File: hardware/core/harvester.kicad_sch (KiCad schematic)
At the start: 28 parts, among them J2 Conn_01x02_Pin, U2 BQ25173DSG, U3 BQ25570, U5 AXP1T34

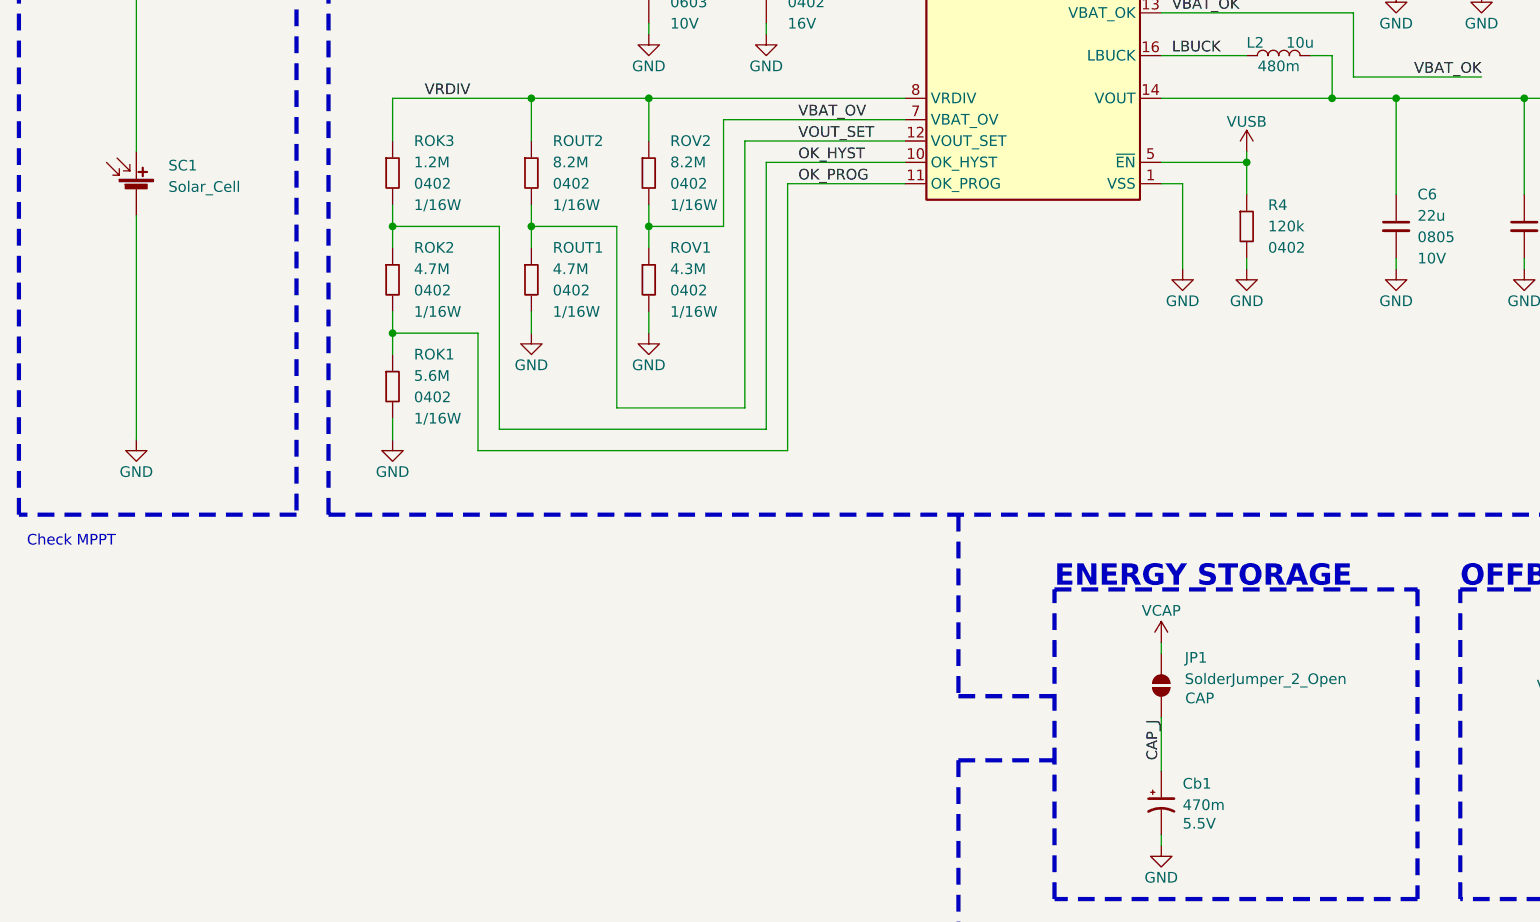
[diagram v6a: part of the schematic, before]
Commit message: updated harvester configuration resistors and removed cap solder link
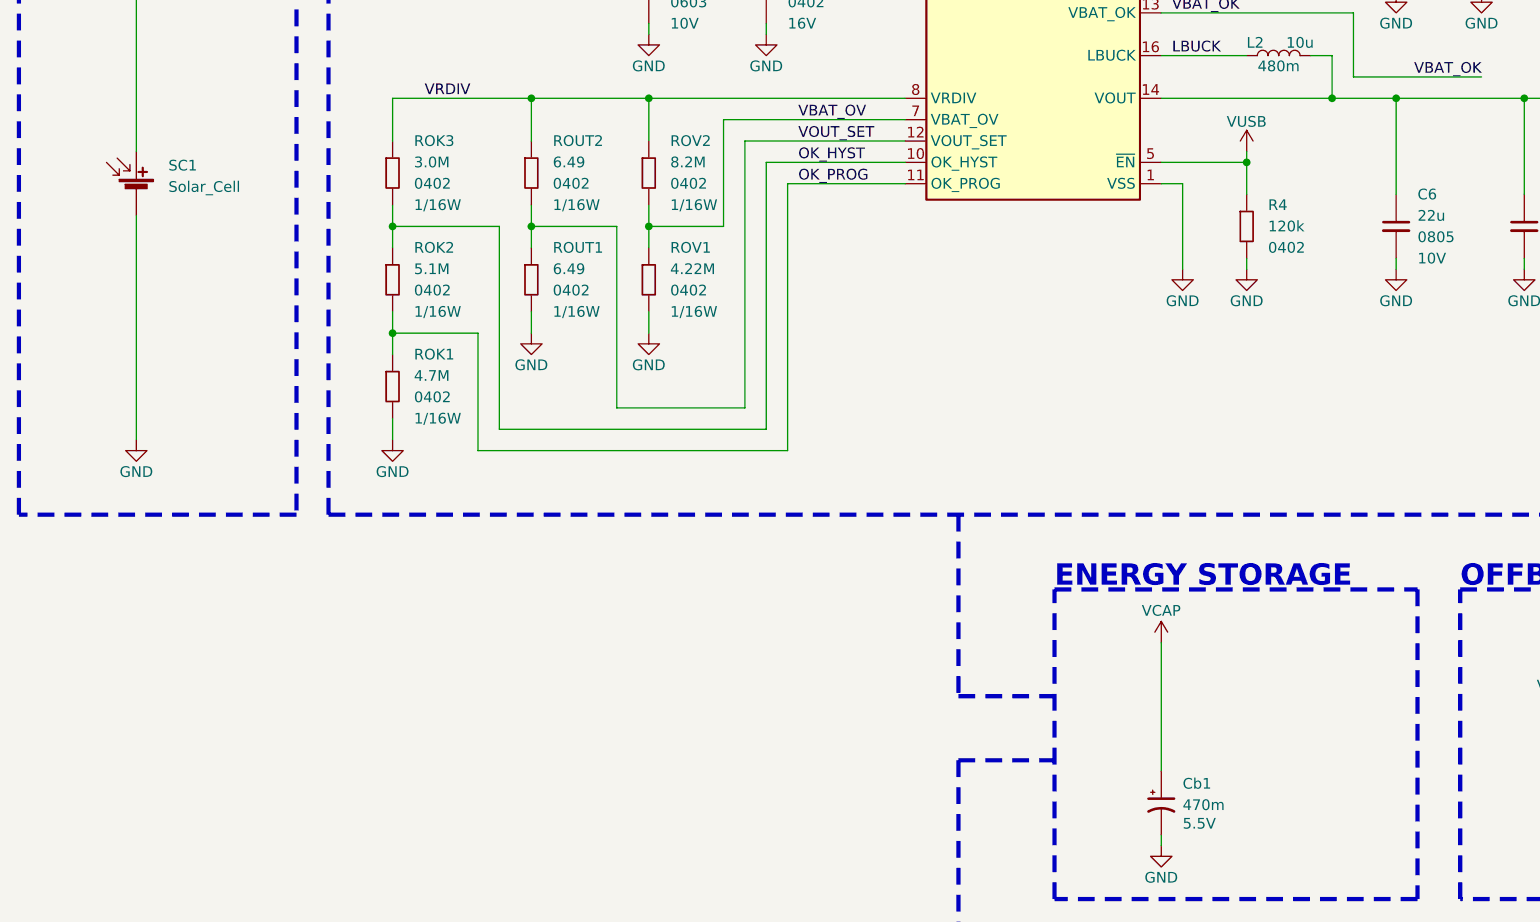
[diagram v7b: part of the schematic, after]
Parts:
- removed JP1: SolderJumper_2_Open, misc:SolderJumper2_Open_0402, symbol misc:SolderJumper_2_Open
- ROK1: value 5.6M -> 4.7M; Part Number RC0402FR-075M6L -> RC0402FR-074M7L
- ROK2: value 4.7M -> 5.1M; Part Number RC0402FR-074M7L -> RC0402FR-075M1L
- ROK3: value 1.2M -> 3.0M; Part Number RC0402FR-071M2L -> RC0402FR-073ML
- ROUT1: value 4.7M -> 6.49; Part Number RC0402FR-074M7L -> RC0402FR-076M49L
- ROUT2: value 8.2M -> 6.49; Part Number RC0402FR-078M2L -> RC0402FR-076M49L
- ROV1: value 4.3M -> 4.22M; Part Number RC0402FR-074M3L -> RC0402FR-074M22L
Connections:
- net CAP_J is gone; now on net VCAP: Cb1.1
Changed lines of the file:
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@@
 		)
 	)
-	(text_box "Check MPPT"
-		(exclude_from_sim no)
-		(at 16.51 107.95 0)
-		(size 92.71 7.62)
-		(margins 0.9525 0.9525 0.9525 0.9525)
-		(stroke
-			(width -0.0001)
-			(type solid)
-		)
-		(fill
-			(type color)
-			(color 255 0 0 1)
-		)
-		(effects
-			(font
-				(size 1.27 1.27)
-				(color 255 255 255 1)
-			)
-			(justify left top)
-		)
-	)
 	(junction
 		(at 161.29 34.29)
@@
 	(wire
 		(pts
-			(xy 152.4 121.92) (xy 152.4 123.19)
+			(xy 152.4 121.92) (xy 152.4 137.16)
 		)
 		(stroke
@@
 	(wire
 		(pts
-			(xy 152.4 130.81) (xy 152.4 137.16)
-		)
-		(stroke
-			(width 0)
-			(type default)
-		)
-	)
-	(wire
-		(pts
 			(xy 60.96 57.15) (xy 60.96 62.23)
 		)
@@
 		)
 	)
-	(label "CAP_J"
-		(at 152.4 135.89 90)
-		(effects
-			(font
-				(size 1.27 1.27)
-			)
-			(justify left bottom)
-		)
-	)
 	(label "VREF_SAMP"
 		(at 109.22 39.37 0)
@@
 			)
 		)
-		(property "Datasheet" ""
+		(property "Datasheet" "https://search.murata.co.jp/Ceramy/image/img/A01X/G101/ENG/GRM155Z71A105KE01-01A.pdf"
 			(at 195.58 68.58 0)
 			(effects
@@
 			)
 		)
-		(property "Datasheet" ""
+		(property "Datasheet" "https://www.yageo.com/upload/media/product/products/datasheet/rchip/PYu-RC_Group_51_RoHS_L_12.pdf"
 			(at 91.44 62.23 0)
 			(effects
@@
 			)
 		)
-		(property "Description" "Capacitor 470mF throug-hole"
+		(property "Description" "Capacitor 470mF through-hole"
 			(at 152.4 137.16 0)
 			(effects
@@
 			)
 		)
-		(property "Value" "8.2M"
+		(property "Value" "6.49"
 			(at 80.01 64.7699 0)
 			(effects
@@
 			)
 		)
-		(property "Datasheet" ""
+		(property "Datasheet" "https://www.yageo.com/upload/media/product/products/datasheet/rchip/PYu-RC_Group_51_RoHS_L_12.pdf"
 			(at 77.47 62.23 0)
 			(effects
@@
 			)
 		)
-		(property "Part Number" "RC0402FR-078M2L"
+		(property "Part Number" "RC0402FR-076M49L"
 			(at 77.47 62.23 0)
 			(effects
@@
 			)
 		)
-		(property "Datasheet" ""
+		(property "Datasheet" "https://www.yageo.com/upload/media/product/products/datasheet/rchip/PYu-RC_Group_51_RoHS_L_12.pdf"
 			(at 153.67 180.34 0)
 			(effects
@@
 			)
 		)
-		(property "Value" "4.3M"
+		(property "Value" "4.22M"
 			(at 93.98 77.4699 0)
 			(effects
@@
 			)
 		)
-		(property "Datasheet" ""
+		(property "Datasheet" "https://www.yageo.com/upload/media/product/products/datasheet/rchip/PYu-RC_Group_51_RoHS_L_12.pdf"
 			(at 91.44 74.93 0)
 			(effects
@@
 			)
 		)
-		(property "Part Number" "RC0402FR-074M3L"
+		(property "Part Number" "RC0402FR-074M22L"
 			(at 91.44 74.93 0)
 			(effects
@@
 			)
 		)
-		(property "Datasheet" ""
+		(property "Datasheet" "https://search.murata.co.jp/Ceramy/image/img/A01X/G101/ENG/GRM188Z71A475ME15-01.pdf"
 			(at 180.34 35.56 0)
 			(effects
@@
 			)
 		)
-		(property "Datasheet" ""
+		(property "Datasheet" "https://mm.digikey.com/Volume0/opasdata/d220001/medias/docus/610/NRS4012T220MDGJ_SS.pdf"
 			(at 101.6 34.29 0)
 			(effects
@@
 			)
 		)
-		(property "Datasheet" ""
+		(property "Datasheet" "https://search.murata.co.jp/Ceramy/image/img/A01X/G101/ENG/GRM188Z71A475ME15-01.pdf"
 			(at 91.44 40.64 0)
 			(effects
@@
 			)
 		)
-		(property "Datasheet" ""
+		(property "Datasheet" "https://www.precidip.com/AppHost/9696,1/Scripts/Modules/Catalog/Default.aspx?c=7&i=223&p=86&pdf=1&dsku=801-PP-NNN-20-001101"
 			(at 210.82 135.89 0)
 			(effects
@@
 			)
 		)
-		(property "Description" "Generic connector, single row, 01x02, script generated"
+		(property "Description" "Right angle 2.54mm connector"
 			(at 210.82 135.89 0)
 			(effects
@@
 			)
 		)
-		(property "Datasheet" ""
+		(property "Datasheet" "https://search.murata.co.jp/Ceramy/image/img/A01X/G101/ENG/GRM155Z71A105KE01-01A.pdf"
 			(at 165.1 180.34 0)
 			(effects
@@
 			)
 		)
-		(property "Description" "Inductor 10u 1008Metric"
+		(property "Description" "Inductor 10u"
 			(at 166.116 56.134 0)
 			(effects
@@
 			)
 		)
-		(property "Value" "5.6M"
+		(property "Value" "4.7M"
 			(at 63.5 90.1699 0)
 			(effects
@@
 			)
 		)
-		(property "Datasheet" ""
+		(property "Datasheet" "https://www.yageo.com/upload/media/product/products/datasheet/rchip/PYu-RC_Group_51_RoHS_L_12.pdf"
 			(at 60.96 87.63 0)
 			(effects
@@
 			)
 		)
-		(property "Part Number" "RC0402FR-075M6L"
+		(property "Part Number" "RC0402FR-074M7L"
 			(at 60.96 87.63 0)
 			(effects
@@
 			)
 		)
-		(property "Datasheet" ""
+		(property "Datasheet" "https://search.murata.co.jp/Ceramy/image/img/A01X/G101/ENG/GRM155Z71A105KE01-01A.pdf"
 			(at 96.52 180.34 0)
 			(effects
@@
 			)
 		)
-		(property "Datasheet" ""
+		(property "Datasheet" "https://search.murata.co.jp/Ceramy/image/img/A01X/G101/ENG/GRM155R71C103KA01-01.pdf"
 			(at 105.41 40.64 0)
 			(effects
@@
 			)
 		)
-		(property "Datasheet" ""
+		(property "Datasheet" "https://www.yageo.com/upload/media/product/products/datasheet/rchip/PYu-RC_Group_51_RoHS_L_12.pdf"
 			(at 153.67 170.18 0)
 			(effects
@@
 			)
 		)
-		(property "Datasheet" ""
+		(property "Datasheet" "https://search.murata.co.jp/Ceramy/image/img/A01X/G101/ENG/GRM21BZ71A226ME15-01.pdf"
 			(at 180.34 68.58 0)
 			(effects
@@
 			)
 		)
-		(property "Value" "4.7M"
+		(property "Value" "5.1M"
 			(at 63.5 77.4699 0)
 			(effects
@@
 			)
 		)
-		(property "Datasheet" ""
+		(property "Datasheet" "https://www.yageo.com/upload/media/product/products/datasheet/rchip/PYu-RC_Group_51_RoHS_L_12.pdf"
 			(at 60.96 74.93 0)
 			(effects
@@
 			)
 		)
-		(property "Part Number" "RC0402FR-074M7L"
+		(property "Part Number" "RC0402FR-075M1L"
 			(at 60.96 74.93 0)
 			(effects
@@
 			)
 		)
-		(property "Value" "1.2M"
+		(property "Value" "3.0M"
 			(at 63.5 64.7699 0)
 			(effects
@@
 			)
 		)
-		(property "Datasheet" ""
+		(property "Datasheet" "https://www.yageo.com/upload/media/product/products/datasheet/rchip/PYu-RC_Group_51_RoHS_L_12.pdf"
 			(at 60.96 62.23 0)
 			(effects
@@
 			)
 		)
-		(property "Part Number" "RC0402FR-071M2L"
+		(property "Part Number" "RC0402FR-073ML"
 			(at 60.96 62.23 0)
 			(effects
@@
 			)
 		)
-		(property "Value" "4.7M"
+		(property "Value" "6.49"
 			(at 80.01 77.4699 0)
 			(effects
@@
 			)
 		)
-		(property "Datasheet" ""
+		(property "Datasheet" "https://www.yageo.com/upload/media/product/products/datasheet/rchip/PYu-RC_Group_51_RoHS_L_12.pdf"
 			(at 77.47 74.93 0)
 			(effects
@@
 			)
 		)
-		(property "Part Number" "RC0402FR-074M7L"
+		(property "Part Number" "RC0402FR-076M49L"
 			(at 77.47 74.93 0)
 			(effects
@@
 			)
 		)
-		(property "Datasheet" ""
+		(property "Datasheet" "https://www.yageo.com/upload/media/product/products/datasheet/rchip/PYu-RC_Group_51_RoHS_L_12.pdf"
 			(at 162.56 68.58 0)
 			(effects
@@
 			)
 		)
-		(property "Datasheet" ""
+		(property "Datasheet" "https://search.murata.co.jp/Ceramy/image/img/A01X/G101/ENG/GRM155R71C103KA01-01.pdf"
 			(at 190.5 35.56 0)
 			(effects
@@
 	)
 	(symbol
-		(lib_id "misc:SolderJumper_2_Open")
-		(at 152.4 127 90)
-		(unit 1)
-		(exclude_from_sim no)
-		(in_bom no)
-		(on_board yes)
-		(dnp no)
-		(property "Reference" "JP1"
-			(at 155.194 123.698 90)
-			(effects
-				(font
-					(size 1.27 1.27)
-				)
-				(justify right)
-			)
-		)
-		(property "Value" "SolderJumper_2_Open"
-			(at 155.194 126.238 90)
-			(effects
-				(font
-					(size 1.27 1.27)
-				)
-				(justify right)
-			)
-		)
-		(property "Footprint" "misc:SolderJumper2_Open_0402"
-			(at 152.4 127 0)
-			(effects
-				(font
-					(size 1.27 1.27)
-				)
-				(hide yes)
-			)
-		)
-		(property "Datasheet" ""
-			(at 152.4 127 0)
-			(effects
-				(font
-					(size 1.27 1.27)
-				)
-				(hide yes)
-			)
-		)
-		(property "Description" "Solder Jumper, 2-pole, open"
-			(at 152.4 127 0)
-			(effects
-				(font
-					(size 1.27 1.27)
-				)
-				(hide yes)
-			)
-		)
-		(property "Short" "CAP"
-			(at 156.972 128.524 90)
-			(effects
-				(font
-					(size 1.27 1.27)
-				)
-			)
-		)
-		(property "Manufacturer" ""
-			(at 152.4 127 90)
-			(effects
-				(font
-					(size 1.27 1.27)
-				)
-				(hide yes)
-			)
-		)
-		(property "Mounting Type" "smt"
-			(at 152.4 127 90)
-			(effects
-				(font
-					(size 1.27 1.27)
-				)
-				(hide yes)
-			)
-		)
-		(pin "1"
-		)
-		(pin "2"
-		)
-		(instances
-			(project ""
-				(path "/8ec7ca4f-74cd-48e1-b45d-8806dcda5073/cd3a3636-14ab-4325-9b35-d239f2fcdaad"
-					(reference "JP1")
-					(unit 1)
-				)
-			)
-		)
-	)
-	(symbol
 		(lib_id "power_symbol:GND")
 		(at 133.35 189.23 0)
@@
 			)
 		)
-		(property "Datasheet" ""
+		(property "Datasheet" "https://www.yageo.com/upload/media/product/products/datasheet/rchip/PYu-RC_Group_51_RoHS_L_12.pdf"
 			(at 139.7 180.34 0)
 			(effects

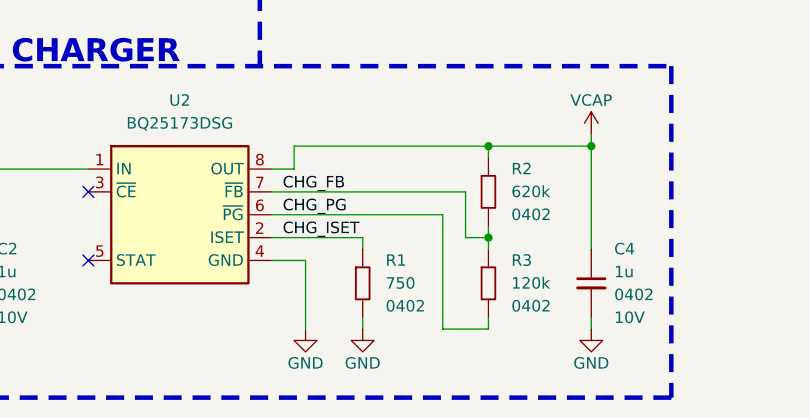
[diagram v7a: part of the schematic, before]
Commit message: Updated charger configuration
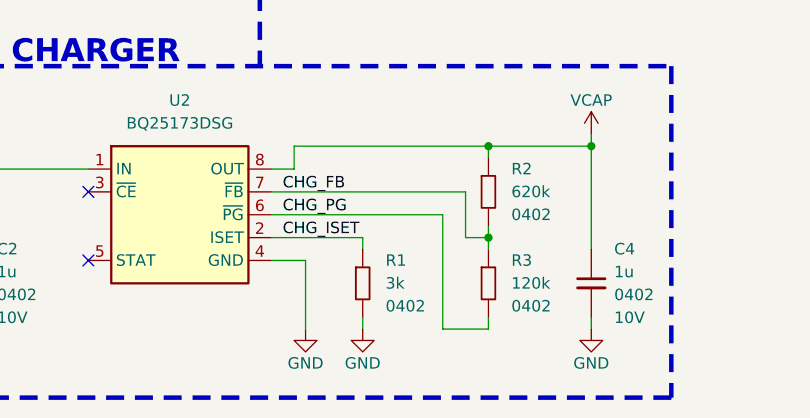
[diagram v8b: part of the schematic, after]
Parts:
- R1: value 750 -> 3k; Part Number RC0402FR-13750RL -> RC0402FR-133KL
